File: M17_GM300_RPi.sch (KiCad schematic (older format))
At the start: 39 parts, among them J1 RJ45, J2 SJ1-3523N, J3 1935161, J4 DB9_Female, J5 RPi Header, Q1 BSS138, Q2 BSS138, Q3 BSS138, Q4 BSS138, SW1 SW_Push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

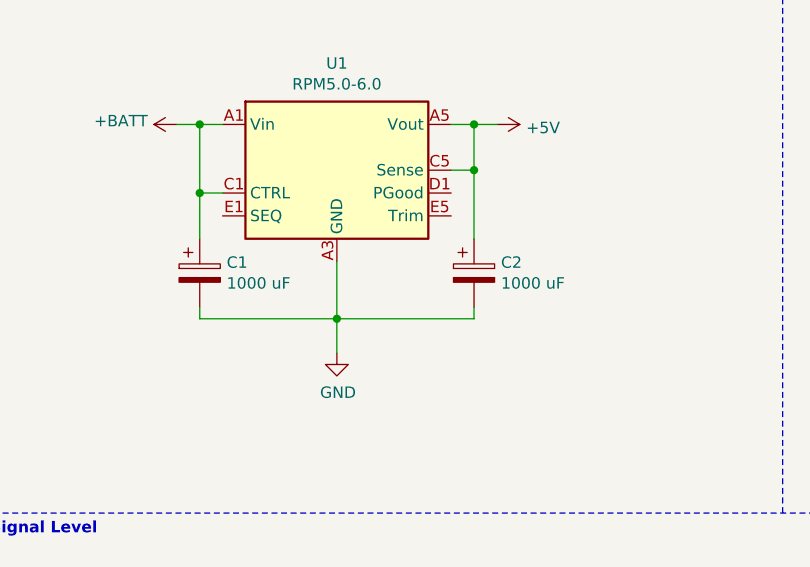
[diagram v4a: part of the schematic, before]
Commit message: change c1 c2, update bom
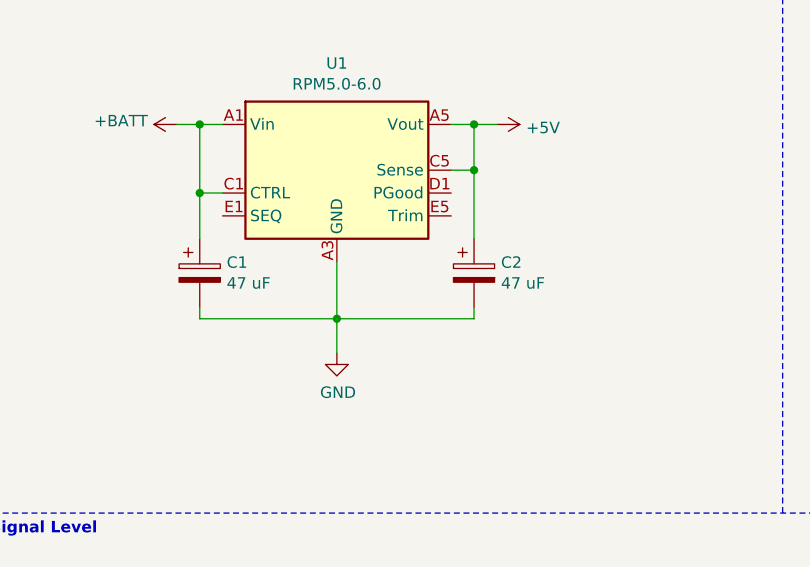
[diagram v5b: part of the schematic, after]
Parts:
- C1, C2: value 1000 uF -> 47 uF
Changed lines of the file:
@@
 P 1950 1850
 F 0 "C1" H 2068 1896 50  0000 L CNN
-F 1 "1000 uF" H 2068 1805 50  0000 L CNN
+F 1 "47 uF" H 2068 1805 50  0000 L CNN
 F 2 "Capacitor_SMD:C_1206_3216Metric_Pad1.33x1.80mm_HandSolder" H 1988 1700 50  0001 C CNN
 F 3 "~" H 1950 1850 50  0001 C CNN
@@
 P 3150 1850
 F 0 "C2" H 3268 1896 50  0000 L CNN
-F 1 "1000 uF" H 3268 1805 50  0000 L CNN
+F 1 "47 uF" H 3268 1805 50  0000 L CNN
 F 2 "Capacitor_SMD:C_1206_3216Metric_Pad1.33x1.80mm_HandSolder" H 3188 1700 50  0001 C CNN
 F 3 "~" H 3150 1850 50  0001 C CNN

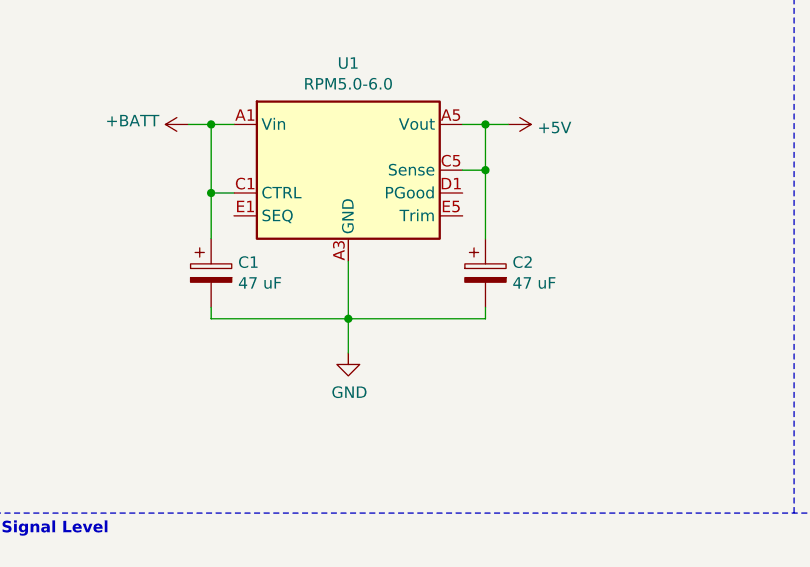
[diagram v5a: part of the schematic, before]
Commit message: change c7, update bom
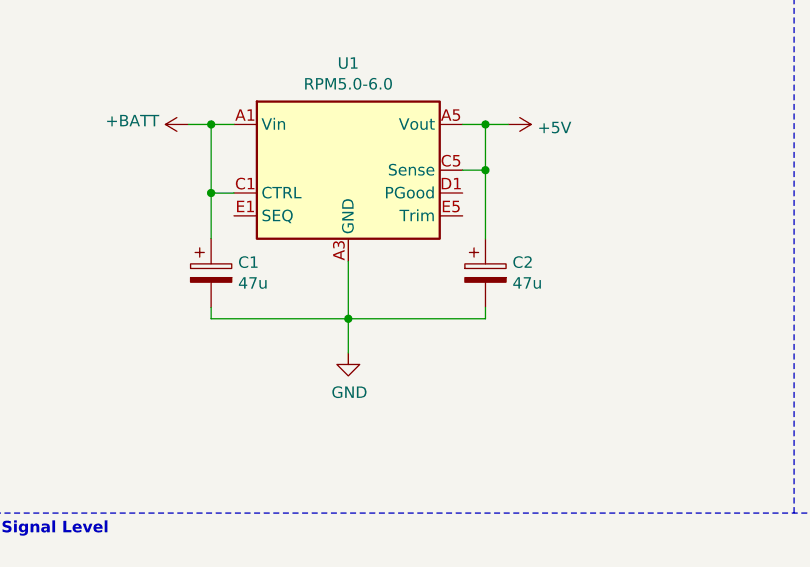
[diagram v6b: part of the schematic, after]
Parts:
- C1, C2: value 47 uF -> 47u
- C6, C7: footprint Capacitor_SMD:C_0805_2012Metric_Pad1.18x1.45mm_HandSolder -> Capacitor_SMD:C_1206_3216Metric_Pad1.33x1.80mm_HandSolder
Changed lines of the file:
@@
 	0    1    1    0
 $EndComp
-$Comp
-L M17_GM300_RPi-rescue:C_Polarized-Device C3
-U 1 1 603EEA67
-P 5600 1300
-F 0 "C3" V 5345 1300 50  0000 C CNN
-F 1 "22u" V 5436 1300 50  0000 C CNN
-F 2 "Capacitor_SMD:C_0805_2012Metric_Pad1.18x1.45mm_HandSolder" H 5638 1150 50  0001 C CNN
-F 3 "~" H 5600 1300 50  0001 C CNN
-	1    5600 1300
-	0    1    1    0
-$EndComp
 Wire Wire Line
 	5750 1300 5850 1300
@@
 F 0 "C7" H 10368 4146 50  0000 L CNN
 F 1 "47u" H 10368 4055 50  0000 L CNN
-F 2 "Capacitor_SMD:C_0805_2012Metric_Pad1.18x1.45mm_HandSolder" H 10288 3950 50  0001 C CNN
+F 2 "Capacitor_SMD:C_1206_3216Metric_Pad1.33x1.80mm_HandSolder" H 10288 3950 50  0001 C CNN
 F 3 "~" H 10250 4100 50  0001 C CNN
 	1    10250 4100
@@
 F 0 "C6" V 9755 5900 50  0000 C CNN
 F 1 "220u" V 9664 5900 50  0000 C CNN
-F 2 "Capacitor_SMD:C_0805_2012Metric_Pad1.18x1.45mm_HandSolder" H 9538 5750 50  0001 C CNN
+F 2 "Capacitor_SMD:C_1206_3216Metric_Pad1.33x1.80mm_HandSolder" H 9538 5750 50  0001 C CNN
 F 3 "~" H 9500 5900 50  0001 C CNN
 	1    9500 5900
@@
 P 1950 1850
 F 0 "C1" H 2068 1896 50  0000 L CNN
-F 1 "47 uF" H 2068 1805 50  0000 L CNN
+F 1 "47u" H 2068 1805 50  0000 L CNN
 F 2 "Capacitor_SMD:C_1206_3216Metric_Pad1.33x1.80mm_HandSolder" H 1988 1700 50  0001 C CNN
 F 3 "~" H 1950 1850 50  0001 C CNN
@@
 P 3150 1850
 F 0 "C2" H 3268 1896 50  0000 L CNN
-F 1 "47 uF" H 3268 1805 50  0000 L CNN
+F 1 "47u" H 3268 1805 50  0000 L CNN
 F 2 "Capacitor_SMD:C_1206_3216Metric_Pad1.33x1.80mm_HandSolder" H 3188 1700 50  0001 C CNN
 F 3 "~" H 3150 1850 50  0001 C CNN
@@
 	9700 850  10250 850
 Connection ~ 9700 850
+$Comp
+L M17_GM300_RPi-rescue:C_Polarized-Device C3
+U 1 1 603EEA67
+P 5600 1300
+F 0 "C3" V 5345 1300 50  0000 C CNN
+F 1 "22u" V 5436 1300 50  0000 C CNN
+F 2 "Capacitor_SMD:C_0805_2012Metric_Pad1.18x1.45mm_HandSolder" H 5638 1150 50  0001 C CNN
+F 3 "~" H 5600 1300 50  0001 C CNN
+	1    5600 1300
+	0    1    1    0
+$EndComp
 $EndSCHEMATC
